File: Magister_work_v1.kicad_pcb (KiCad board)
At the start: 4 copper layers, 80 x 80 mm, 164 parts, among them J1 USB_B_Mini, J2 Conn_01x03_Pin, J3 Conn_01x03_Pin, J4 Conn_01x02_Pin, J5 Conn_01x02_Pin, J6 Conn_01x04_Pin, J7 Conn_01x06_Pin, J8 Conn_01x04_Pin, J9 Conn_01x02_Pin, Q1 AO3400A, Q2 AO3400A, SW1 SW_Push, SW10 SW_Push, SW11 SW_Push, SW12 SW_Push, SW2 SW_Push, SW3 SW_Push, SW4 SW_Push, SW5 SW_Push, SW6 SW_Push, SW7 SW_Push, SW8 SW_Push, SW9 SW_Push, U1 AMS1117-3.3, U2 SRV05-4, U3 STM32F407VETx, U4 Ai-Thinker-Ra-01, U5 AT24C256, U6 Ai-Thinker-Ra-01SH, U7 ULN2003, U8 ULN2003, U9 74HC165, Y1 X322525MQB4SI, Y2 SMD03215C2

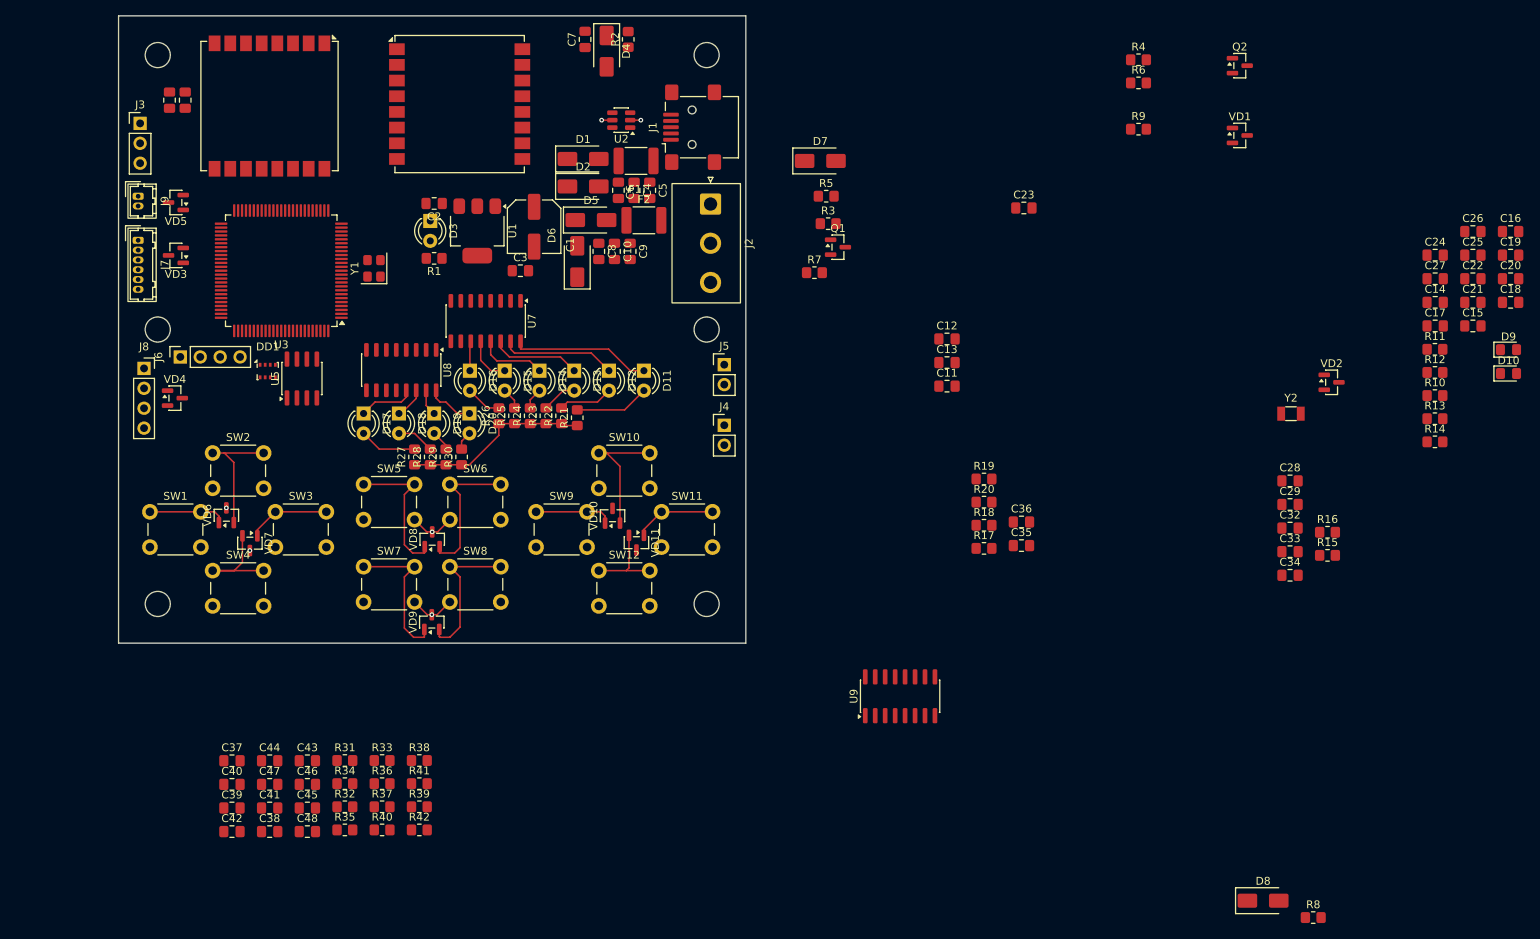
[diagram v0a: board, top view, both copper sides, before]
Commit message: feat: добавлена обвязка внешних интерфейсов
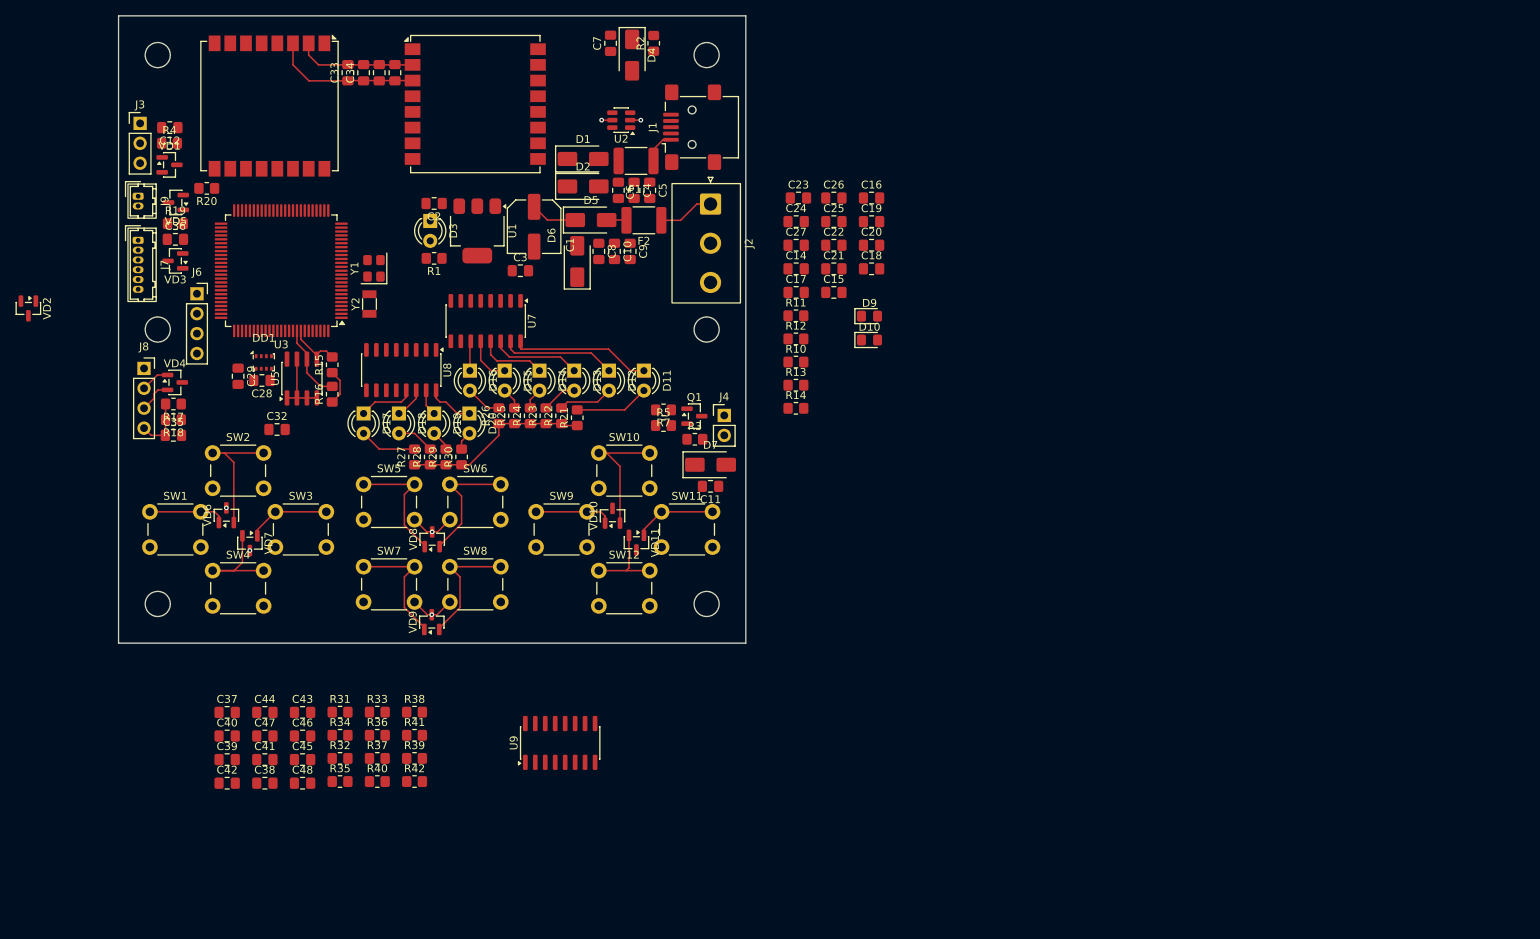
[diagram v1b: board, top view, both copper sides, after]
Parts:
- removed C13: 0.1u, Capacitor_SMD:C_0805_2012Metric_Pad1.18x1.45mm_HandSolder
- removed D8: SMAJ5.0CA, Diode_SMD:D_SMA
- removed J5: Conn_01x02_Pin, Connector_PinHeader_2.54mm:PinHeader_1x02_P2.54mm_Vertical
- removed Q2: AO3400A, Package_TO_SOT_SMD:SOT-23
- removed R6: 0, Resistor_SMD:R_0805_2012Metric_Pad1.20x1.40mm_HandSolder
- removed R8: 100, Resistor_SMD:R_0805_2012Metric_Pad1.20x1.40mm_HandSolder
- removed R9: 10k, Resistor_SMD:R_0805_2012Metric_Pad1.20x1.40mm_HandSolder
- moved VD2 166.5 mm to (18.5, 67.3), turned to -90 degrees
- moved VD1 136.6 mm to (36.5, 49.0)
- moved C29 135.1 mm to (45.2, 76.0), turned to -90 degrees
- moved C33 134.8 mm to (59.2, 37.2), turned to 90 degrees
- moved C34 134.4 mm to (61.2, 37.2), turned to 90 degrees
- moved C28 131.7 mm to (48.3, 76.5), turned to 180 degrees
- moved C32 129.8 mm to (50.2, 82.8)
- moved R15 129.2 mm to (57.2, 74.5), turned to 90 degrees
- moved R16 128.2 mm to (57.2, 78.2), turned to 90 degrees
- moved R4 124.0 mm to (36.5, 46.2)
- moved Y2 118.4 mm to (62.0, 66.8), turned to 90 degrees
- moved C36 113.8 mm to (37.2, 58.5)
- moved C35 109.1 mm to (37.0, 83.5)
- moved R19 108.1 mm to (37.2, 56.5)
- moved R20 106.9 mm to (41.2, 52.0), turned to 180 degrees
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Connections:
- C29 pad 1: +3V3A -> +3V3D
- DD1 pad 8: +3V3A -> +3V3D
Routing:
- net GND: track 13.0 -> 37.0 mm
- net +3V3D: track 0.00 -> 23.4 mm
- net EEPROM_SCL: track 0.00 -> 9.82 mm
- net EEPROM_SDA: track 0.00 -> 7.47 mm
- net Net-(F2-A1): track 0.00 -> 7.13 mm
- net Net-(J8-Pin_4): track 0.00 -> 7.11 mm
- net +5V: track 25.3 -> 31.2 mm
- net DEBUG_TX1: track 0.00 -> 4.29 mm
- net Net-(F1-A1): track 0.00 -> 4.21 mm
- net DEBUG_RX1: track 0.00 -> 3.70 mm
- net Net-(VD9-K1): track 18.9 -> 15.8 mm
- net Net-(VD9-K2): track 18.9 -> 15.8 mm
- net Net-(VD8-K2): track 18.8 -> 16.2 mm
- net Net-(D5-A): track 0.00 -> 2.54 mm
- net Net-(VD8-K1): track 18.6 -> 16.1 mm

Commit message: feat: разведена обвыязка кнопок
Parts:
- removed U9: 74HC165, Package_SO:SOIC-16_3.9x9.9mm_P1.27mm
- moved C48 65.1 mm to (106.2, 89.8), turned to 90 degrees
- moved C45 60.1 mm to (102.2, 89.8), turned to 90 degrees
- moved R42 52.6 mm to (104.2, 89.8), turned to -90 degrees
- moved C47 49.8 mm to (86.8, 89.8), turned to 90 degrees
- moved R39 47.7 mm to (100.2, 89.8), turned to -90 degrees
- moved C44 44.8 mm to (82.8, 89.7), turned to 90 degrees
- moved C42 44.4 mm to (65.8, 89.2), turned to 90 degrees
- moved C46 42.2 mm to (80.2, 89.2), turned to 90 degrees
- moved R40 41.4 mm to (78.2, 89.2), turned to -90 degrees
- moved C39 39.9 mm to (61.8, 89.2), turned to 90 degrees
- moved C38 38.4 mm to (53.0, 89.7), turned to 90 degrees
- moved R41 38.3 mm to (88.8, 89.7), turned to -90 degrees
- moved R35 38.1 mm to (55.0, 89.7), turned to -90 degrees
- moved C43 37.4 mm to (76.2, 89.2), turned to 90 degrees
- moved R37 37.2 mm to (74.2, 89.2), turned to -90 degrees
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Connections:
- C42 pad 2: DI6 -> DI7
- C43 pad 2: DI7 -> DI6
- R36 pad 1: DI6 -> DI7
- R36 pad 2: Net-(VD8-K2) -> Net-(VD9-K1)
- R37 pad 1: DI7 -> DI6
- R37 pad 2: Net-(VD9-K1) -> Net-(VD8-K2)
- SW6 pad 1: Net-(VD8-K2) -> Net-(VD9-K1)
- SW7 pad 1: Net-(VD9-K1) -> Net-(VD8-K2)
- VD9 pad 3: GND -> unconnected-(VD9-A-Pad3)
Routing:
- net Net-(VD11-K2): track 11.1 -> 25.3 mm
- net Net-(VD7-K2): track 14.1 -> 28.2 mm
- net Net-(D7-A2): track 0.00 -> 9.96 mm
- net Net-(VD9-K2): track 15.8 -> 22.4 mm
- net Net-(VD6-K2): track 15.9 -> 21.9 mm
- net Net-(VD10-K2): track 17.1 -> 23.1 mm
- net Net-(VD9-K1): track 15.8 -> 21.6 mm
- net Net-(VD8-K1): track 16.1 -> 11.7 mm
- net Net-(VD8-K2): track 16.2 -> 11.9 mm
- net Net-(Q1-G): track 0.00 -> 4.06 mm
- net Net-(VD10-K1): track 9.92 -> 13.1 mm
- net Net-(VD6-K1): track 9.85 -> 13.0 mm
- net Net-(VD7-K1): track 10.5 -> 13.5 mm
- net Net-(VD11-K1): track 10.4 -> 13.3 mm
- net Net-(J4-Pin_1): track 0.00 -> 2.91 mm
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
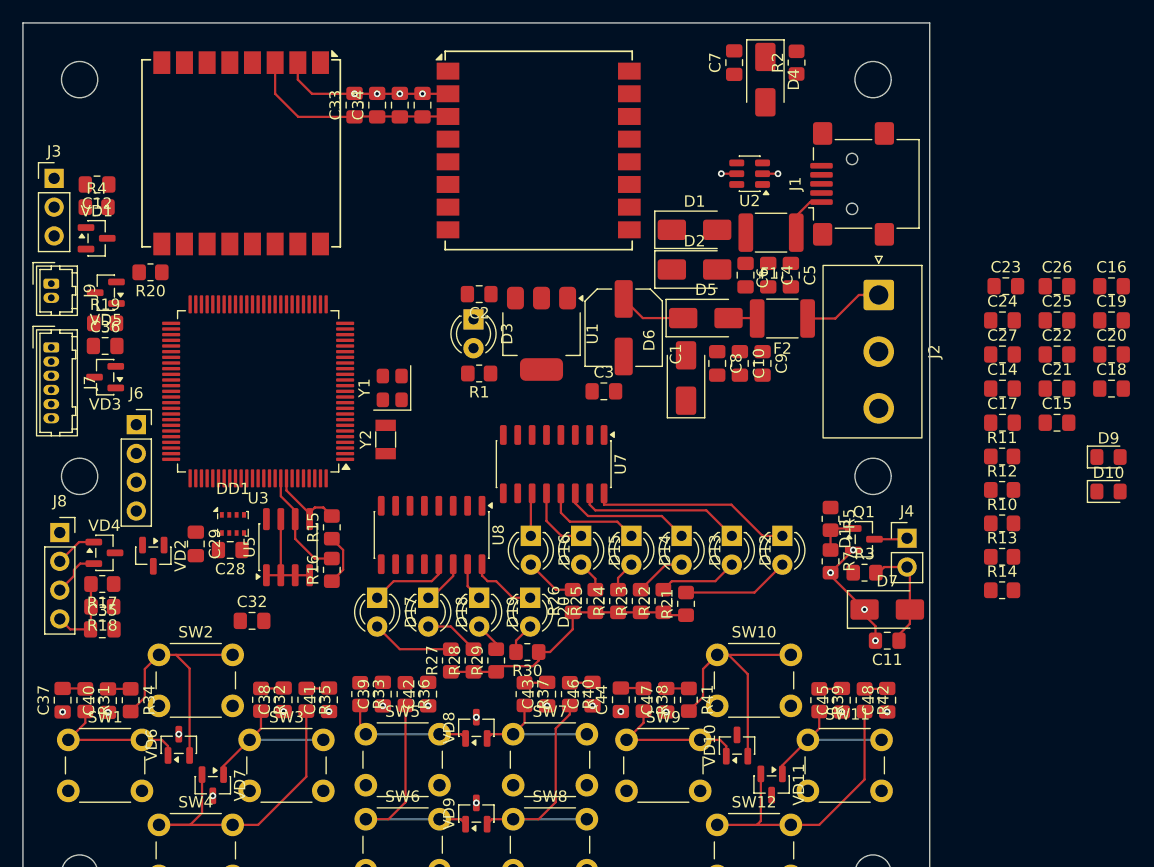
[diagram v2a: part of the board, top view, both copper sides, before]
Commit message: feat: размешены все компоненты на печатной плате
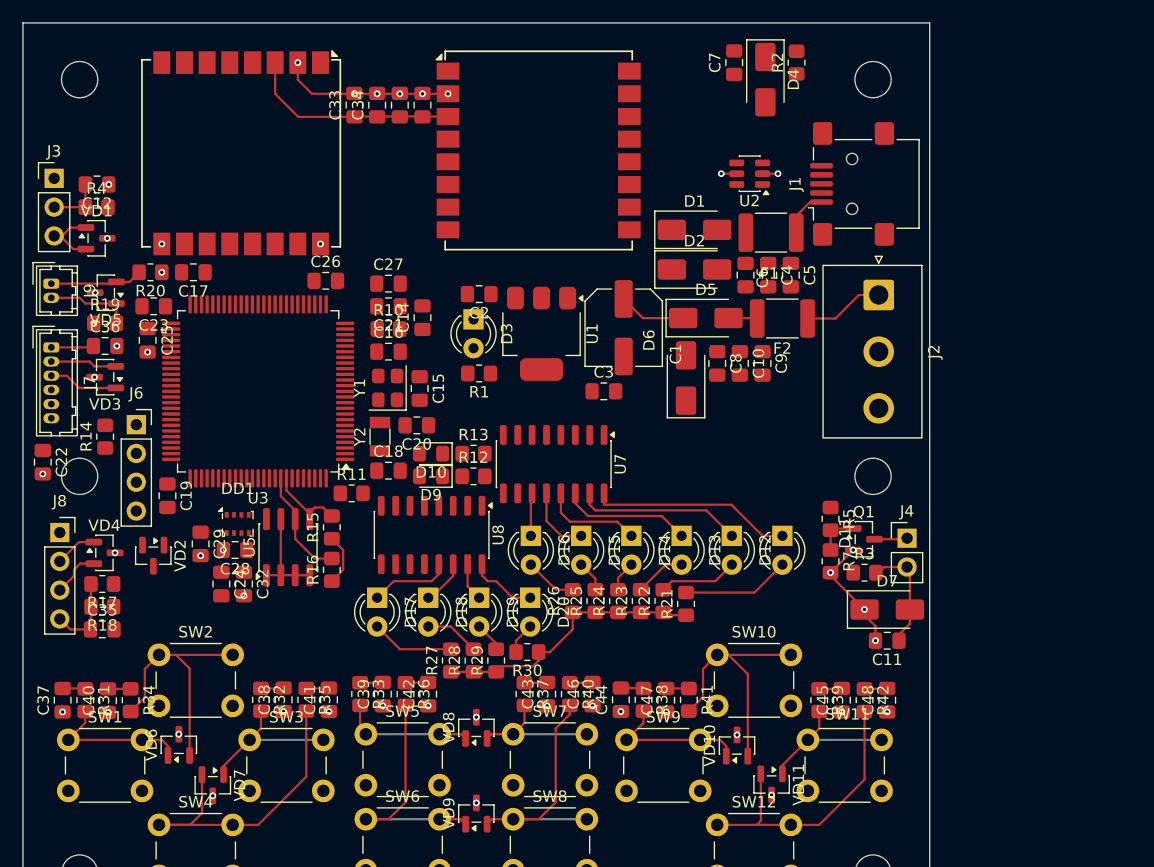
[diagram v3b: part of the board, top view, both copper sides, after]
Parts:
- moved C22 90.0 mm to (31.8, 68.8), turned to -90 degrees
- moved C19 84.7 mm to (42.8, 71.7), turned to -90 degrees
- moved R14 80.3 mm to (37.2, 66.5), turned to 90 degrees
- moved C25 80.2 mm to (41.0, 58.0), turned to -90 degrees
- moved C23 75.2 mm to (41.5, 55.0), turned to 180 degrees
- moved C24 72.7 mm to (47.5, 79.5), turned to -90 degrees
- moved C17 72.6 mm to (45.0, 52.0), turned to 180 degrees
- moved C26 64.5 mm to (56.7, 52.8)
- moved C18 64.2 mm to (62.2, 69.5)
- moved C16 64.0 mm to (62.2, 59.0)
- moved C20 61.6 mm to (64.8, 65.5), turned to 180 degrees
- moved D10 59.9 mm to (66.0, 68.0), turned to 180 degrees
- moved D9 59.8 mm to (66.0, 70.0), turned to 180 degrees
- moved C21 59.4 mm to (62.2, 55.0), turned to 180 degrees
- moved R11 57.5 mm to (59.0, 71.5)
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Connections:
- C21 pad 2: +3V3A -> +3V3
- C22 pad 1: +3V3D -> +3V3
- C23 pad 1: +3V3D -> +3V3
- C24 pad 1: +3V3D -> +3V3
- C25 pad 1: +3V3D -> +3V3
- C26 pad 1: +3V3D -> +3V3
- C27 pad 1: +3V3D -> +3V3
- C28 pad 1: +3V3D -> +3V3
- C29 pad 1: +3V3D -> +3V3
- C30 pad 1: +3V3D -> +3V3
- C31 pad 1: +3V3D -> +3V3
- C32 pad 1: +3V3D -> +3V3
- C33 pad 1: +3V3D -> +3V3
- C34 pad 1: +3V3D -> +3V3
- DD1 pad 6: +3V3D -> +3V3
- DD1 pad 8: +3V3D -> +3V3
- R10 pad 1: +3V3D -> +3V3
- R12 pad 2: +3V3D -> +3V3
- R13 pad 2: +3V3D -> +3V3
- R14 pad 1: +3V3D -> +3V3
- R15 pad 1: +3V3D -> +3V3
- R16 pad 1: +3V3D -> +3V3
- R19 pad 1: +3V3D -> +3V3
- R20 pad 1: +3V3D -> +3V3
- U3 pad 100: +3V3D -> +3V3
- U3 pad 11: +3V3D -> +3V3
- U3 pad 19: +3V3D -> +3V3
- U3 pad 21: +3V3A -> +3V3
- U3 pad 22: +3V3A -> +3V3
- U3 pad 28: +3V3D -> +3V3
- U3 pad 50: +3V3D -> +3V3
- U3 pad 6: +3V3D -> +3V3
- U3 pad 75: +3V3D -> +3V3
- U4 pad 3: +3V3D -> +3V3
- U5 pad 8: +3V3D -> +3V3
- U6 pad 3: +3V3D -> +3V3
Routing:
- net +3V3D: track 23.4 -> 0.00 mm
- net +3V3: track 0.00 -> 23.4 mm, vias 0 -> 2
- net BN_880_SDA: track 0.00 -> 8.16 mm
- net BN_880_SCL: track 0.00 -> 7.71 mm
- net PWM1: track 0.00 -> 6.41 mm
- net BN_880_RX: track 0.00 -> 6.13 mm
- net BN_880_TX: track 0.00 -> 5.86 mm
- net Net-(J3-Pin_2): track 0.00 -> 4.75 mm
- net +5V: track 31.7 -> 35.4 mm
- net DI7: track 0.00 -> 2.02 mm
- net DI5: track 0.00 -> 2.02 mm
- net GND: vias 24 -> 41

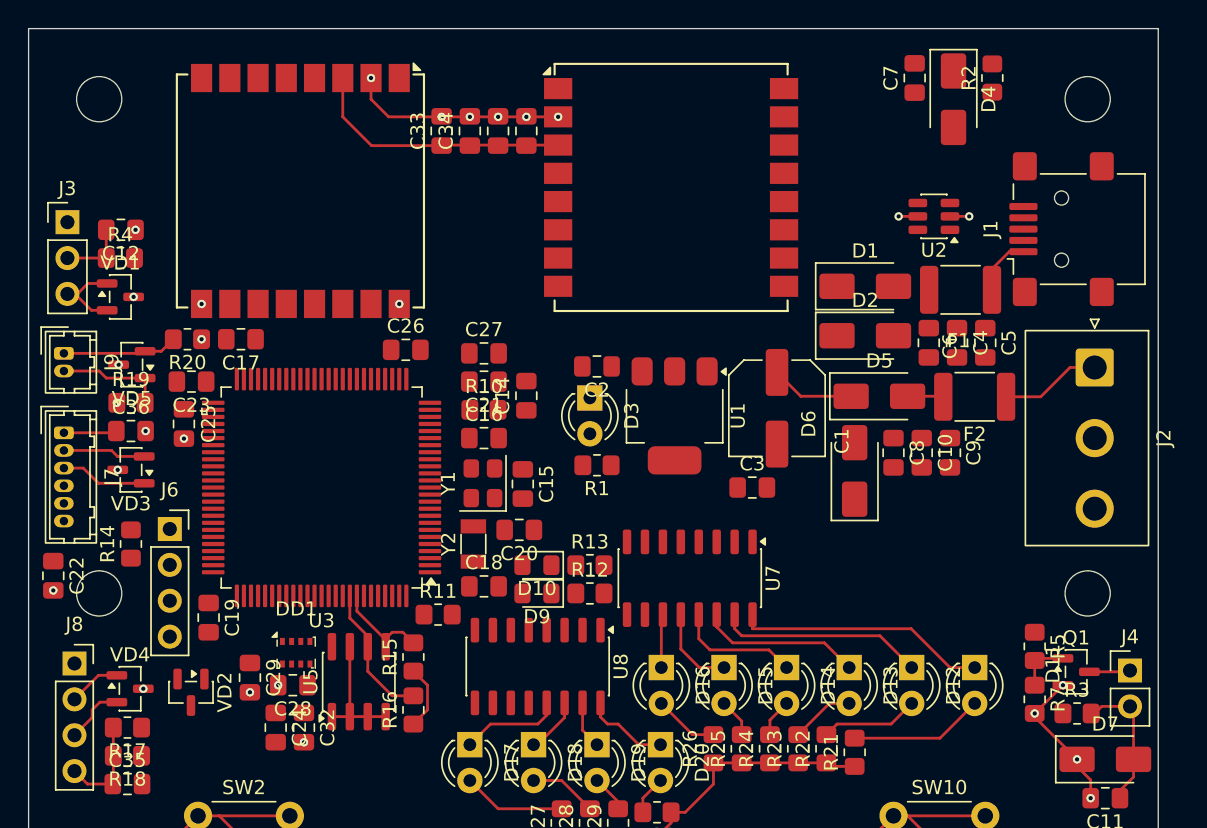
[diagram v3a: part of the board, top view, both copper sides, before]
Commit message: feat: начата разводка сигнальных линий и линий питания
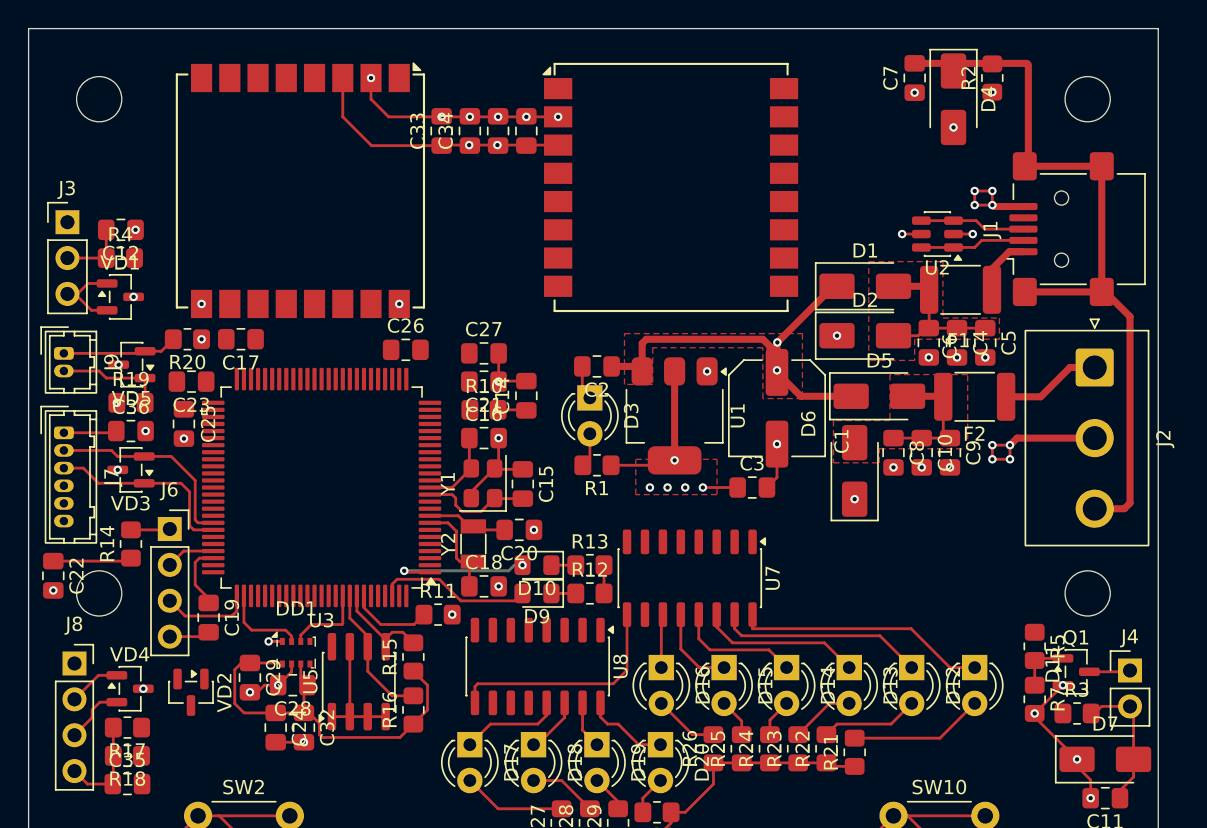
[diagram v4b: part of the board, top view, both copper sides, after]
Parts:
- moved U2 1.27 mm to (94.4, 44.5)
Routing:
- net PE: track 0.00 -> 55.0 mm
- net +3V3: track 23.4 -> 68.7 mm, vias 2 -> 9
- net GND: track 35.9 -> 80.3 mm, vias 41 -> 68
- net +5V: track 35.4 -> 75.5 mm, vias 1 -> 3
- net +5V_in: track 0.00 -> 12.1 mm
- net Net-(D9-A): track 0.00 -> 11.0 mm
- net Net-(D10-A): track 0.00 -> 10.4 mm, vias 0 -> 2
- net BN_880_TX: track 5.86 -> 14.3 mm
- net /STMF401_Sheet/HSE_IN: track 0.00 -> 7.77 mm
- net BN_880_RX: track 6.13 -> 13.8 mm
- net D+: track 0.00 -> 7.47 mm
- net D-: track 0.00 -> 7.43 mm
- net /STMF401_Sheet/LSE_IN: track 0.00 -> 7.20 mm
- net Net-(D5-A): track 2.54 -> 9.66 mm
- net /STMF401_Sheet/SWCLK: track 0.00 -> 6.42 mm
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- added copper zone on F.Cu, net +3V3
- added copper zone on F.Cu, net +5V
- added copper zone on F.Cu, net +5V_in
- added copper zone on F.Cu, net Net-(D5-A)
